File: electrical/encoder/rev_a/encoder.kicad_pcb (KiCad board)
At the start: 2 copper layers, 19.8 x 45.5 mm, 1 part, among them CN1 HR2_Encoder;HR2Encoder

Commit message: Finally have everything fitting together.
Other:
- board size 19.8 x 45.5 mm -> 14.8 x 40.4 mm

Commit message: Started working on encdoer PCB.
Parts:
- added Q1: AH1806;SC59, HR2:SC59, F.Cu at (101.1, 81.0)
- CN1: value HR2_Encoder;HR2Encoder -> ENCODER;2xM1x3RA; footprint HR2:Encoder -> HR2:ENCODER_2xM1x3RA
- moved CN1 3.31 mm to (96.7, 100.3)
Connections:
- CN1 pad 1: (no net) -> Net-(CN1-Pad1)
- CN1 pad 2: (no net) -> Net-(CN1-Pad2)
- CN1 pad 3: (no net) -> Net-(CN1-Pad3)
- CN1 pad 4: (no net) -> Net-(CN1-Pad4)
- CN1 pad 5: (no net) -> Net-(CN1-Pad5)
- CN1 pad 6: (no net) -> Net-(CN1-Pad6)
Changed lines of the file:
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@@
-(kicad_pcb (version 20171130) (host pcbnew 5.1.6-c6e7f7d~86~ubuntu18.04.1)
+(kicad_pcb (version 20171130) (host pcbnew 5.1.6-c6e7f7d~87~ubuntu18.04.1)
   (general
     (thickness 1.6)
@@
     (tracks 0)
     (zones 0)
-    (modules 1)
-    (nets 1)
+    (modules 2)
+    (nets 10)
   )
   (page A4)
@@
   )
   (net 0 "")
+  (net 1 "Net-(CN1-Pad3)")
+  (net 2 "Net-(CN1-Pad2)")
+  (net 3 "Net-(CN1-Pad1)")
+  (net 4 "Net-(CN1-Pad6)")
+  (net 5 "Net-(CN1-Pad5)")
+  (net 6 "Net-(CN1-Pad4)")
+  (net 7 "Net-(Q1-Pad2)")
+  (net 8 "Net-(Q1-Pad1)")
+  (net 9 "Net-(Q1-Pad3)")
   (net_class Default "This is the default net class."
     (clearance 0.2)
@@
     (uvia_dia 0.3)
     (uvia_drill 0.1)
+    (add_net "Net-(CN1-Pad1)")
+    (add_net "Net-(CN1-Pad2)")
+    (add_net "Net-(CN1-Pad3)")
+    (add_net "Net-(CN1-Pad4)")
+    (add_net "Net-(CN1-Pad5)")
+    (add_net "Net-(CN1-Pad6)")
+    (add_net "Net-(Q1-Pad1)")
+    (add_net "Net-(Q1-Pad2)")
+    (add_net "Net-(Q1-Pad3)")
   )
-  (module HR2:Encoder (layer F.Cu)
-    (at 100.00 100.00)
-    (fp_text reference CN1 (at -10.7 20.5) (layer F.SilkS)
+  (module HR2:SC59 (layer F.Cu)
+    (at 101.101623 80.969999)
+    (fp_text reference Q1 (at 1.27 7.62) (layer F.SilkS)
+      (effects (font (size 1 1) (thickness 0.15)))
+    )
+    (fp_text value AH1806;SC59 (at 0 -11.43) (layer F.Fab)
+      (effects (font (size 1 1) (thickness 0.15)))
+    )
+    (fp_line (start -1.5 -0.8) (end -1.5 0.8) (layer F.SilkS) (width 0.1))
+    (fp_line (start -1.5 -0.8) (end 1.5 -0.8) (layer F.SilkS) (width 0.1))
+    (fp_line (start -1.5 0.8) (end 1.5 0.8) (layer F.SilkS) (width 0.1))
+    (fp_line (start 1.5 -0.8) (end 1.5 0.8) (layer F.SilkS) (width 0.1))
+    (fp_circle (center -1.67 0.94) (end -1.66 0.91) (layer F.SilkS) (width 0.1))
+    (pad 2 smd rect (at 0 -1.2) (size 0.8 1) (layers F.Cu F.Paste F.Mask)
+      (net 7 "Net-(Q1-Pad2)"))
+    (pad 1 smd rect (at -0.95 1.2) (size 0.8 1) (layers F.Cu F.Paste F.Mask)
+      (net 8 "Net-(Q1-Pad1)"))
+    (pad 3 smd rect (at 0.95 1.2) (size 0.8 1) (layers F.Cu F.Paste F.Mask)
+      (net 9 "Net-(Q1-Pad3)"))
+  )
+  (module HR2:ENCODER_2xM1x3RA (layer F.Cu)
+    (at 96.7 100.3)
+    (fp_text reference CN1 (at 0 -2) (layer F.SilkS)
       (effects (font (size 1 1) (thickness 0.2)))
     )
-    (fp_text value HR2_Encoder;HR2Encoder (at 0 -2) (layer F.Fab)
+    (fp_text value ENCODER;2xM1x3RA (at 0 0) (layer F.Fab)
       (effects (font (size 1 1) (thickness 0.2)))
     )
-    (fp_line (start -5.5731 -21.46) (end -3.0331 -21.46) (layer B.SilkS) (width 0.2))
-    (fp_line (start -3.0331 -21.46) (end -3.0331 -13.84) (layer B.SilkS) (width 0.2))
-    (fp_line (start -3.0331 -13.84) (end -5.5731 -13.84) (layer B.SilkS) (width 0.2))
-    (fp_line (start -5.5731 -13.84) (end -5.5731 -21.46) (layer B.SilkS) (width 0.2))
-    (fp_line (start -6.7181 -15.11) (end -5.5731 -15.11) (layer B.SilkS) (width 0.2))
-    (fp_line (start -6.7181 -17.65) (end -5.5731 -17.65) (layer B.SilkS) (width 0.2))
-    (fp_line (start -6.7181 -20.19) (end -5.5731 -20.19) (layer B.SilkS) (width 0.2))
-    (fp_line (start -9.3851 -13.305) (end -9.4558 -13.2757) (layer B.SilkS) (width 0.2))
-    (fp_line (start -9.4558 -13.2757) (end -9.4851 -13.205) (layer B.SilkS) (width 0.2))
-    (fp_line (start -9.4851 -13.205) (end -9.4558 -13.1343) (layer B.SilkS) (width 0.2))
-    (fp_line (start -9.4558 -13.1343) (end -9.3851 -13.105) (layer B.SilkS) (width 0.2))
-    (fp_line (start -9.3851 -13.105) (end -9.3144 -13.1343) (layer B.SilkS) (width 0.2))
-    (fp_line (start -9.3144 -13.1343) (end -9.2851 -13.205) (layer B.SilkS) (width 0.2))
-    (fp_line (start -9.2851 -13.205) (end -9.3144 -13.2757) (layer B.SilkS) (width 0.2))
-    (fp_line (start -9.3144 -13.2757) (end -9.3851 -13.305) (layer B.SilkS) (width 0.2))
-    (fp_line (start -5.5731 13.84) (end -3.0331 13.84) (layer B.SilkS) (width 0.2))
-    (fp_line (start -3.0331 13.84) (end -3.0331 21.46) (layer B.SilkS) (width 0.2))
-    (fp_line (start -3.0331 21.46) (end -5.5731 21.46) (layer B.SilkS) (width 0.2))
-    (fp_line (start -5.5731 21.46) (end -5.5731 13.84) (layer B.SilkS) (width 0.2))
-    (fp_line (start -6.7181 20.19) (end -5.5731 20.19) (layer B.SilkS) (width 0.2))
-    (fp_line (start -6.7181 17.65) (end -5.5731 17.65) (layer B.SilkS) (width 0.2))
-    (fp_line (start -6.7181 15.11) (end -5.5731 15.11) (layer B.SilkS) (width 0.2))
-    (fp_line (start -9.3851 21.995) (end -9.4558 22.0243) (layer B.SilkS) (width 0.2))
-    (fp_line (start -9.4558 22.0243) (end -9.4851 22.095) (layer B.SilkS) (width 0.2))
-    (fp_line (start -9.4851 22.095) (end -9.4558 22.1657) (layer B.SilkS) (width 0.2))
-    (fp_line (start -9.4558 22.1657) (end -9.3851 22.195) (layer B.SilkS) (width 0.2))
-    (fp_line (start -9.3851 22.195) (end -9.3144 22.1657) (layer B.SilkS) (width 0.2))
-    (fp_line (start -9.3144 22.1657) (end -9.2851 22.095) (layer B.SilkS) (width 0.2))
-    (fp_line (start -9.2851 22.095) (end -9.3144 22.0243) (layer B.SilkS) (width 0.2))
-    (fp_line (start -9.3144 22.0243) (end -9.3851 21.995) (layer B.SilkS) (width 0.2))
-    (pad 7 thru_hole oval (at 0 6.6252) (size 3.3 1.7) (drill oval 2.6 0.9) (layers *.Cu *.Mask))
-    (pad 8 thru_hole oval (at 0 -6.6248) (size 3.3 1.7) (drill oval 2.6 0.9) (layers *.Cu *.Mask))
-    (pad 1 thru_hole circle (at -7.4801 20.19) (size 1.5 1.5) (drill 1) (layers *.Cu *.Mask))
-    (pad 2 thru_hole circle (at -7.4801 17.65) (size 1.5 1.5) (drill 1) (layers *.Cu *.Mask))
-    (pad 3 thru_hole circle (at -7.4801 15.11) (size 1.5 1.5) (drill 1) (layers *.Cu *.Mask))
-    (pad 4 thru_hole circle (at -7.4801 -15.11) (size 1.5 1.5) (drill 1) (layers *.Cu *.Mask))
-    (pad 5 thru_hole circle (at -7.4801 -17.65) (size 1.5 1.5) (drill 1) (layers *.Cu *.Mask))
-    (pad 6 thru_hole circle (at -7.4801 -20.19) (size 1.5 1.5) (drill 1) (layers *.Cu *.Mask))
+    (fp_line (start -9.39 -12.57) (end -11.93 -12.57) (layer B.SilkS) (width 0.2))
+    (fp_line (start -11.93 -12.57) (end -11.93 -20.19) (layer B.SilkS) (width 0.2))
+    (fp_line (start -11.93 -20.19) (end -9.39 -20.19) (layer B.SilkS) (width 0.2))
+    (fp_line (start -9.39 -20.19) (end -9.39 -12.57) (layer B.SilkS) (width 0.2))
+    (fp_line (start -8.24 -18.92) (end -9.39 -18.92) (layer B.SilkS) (width 0.2))
+    (fp_line (start -8.24 -16.38) (end -9.39 -16.38) (layer B.SilkS) (width 0.2))
+    (fp_line (start -8.24 -13.84) (end -9.39 -13.84) (layer B.SilkS) (width 0.2))
+    (fp_line (start -8.75 -20.73) (end -8.68 -20.75) (layer B.SilkS) (width 0.2))
+    (fp_line (start -8.68 -20.75) (end -8.65 -20.83) (layer B.SilkS) (width 0.2))
+    (fp_line (start -8.65 -20.83) (end -8.68 -20.9) (layer B.SilkS) (width 0.2))
+    (fp_line (start -8.68 -20.9) (end -8.75 -20.93) (layer B.SilkS) (width 0.2))
+    (fp_line (start -8.75 -20.93) (end -8.82 -20.9) (layer B.SilkS) (width 0.2))
+    (fp_line (start -8.82 -20.9) (end -8.85 -20.83) (layer B.SilkS) (width 0.2))
+    (fp_line (start -8.85 -20.83) (end -8.82 -20.75) (layer B.SilkS) (width 0.2))
+    (fp_line (start -8.82 -20.75) (end -8.75 -20.73) (layer B.SilkS) (width 0.2))
+    (fp_line (start -9.39 20.19) (end -11.93 20.19) (layer B.SilkS) (width 0.2))
+    (fp_line (start -11.93 20.19) (end -11.93 12.57) (layer B.SilkS) (width 0.2))
+    (fp_line (start -11.93 12.57) (end -9.39 12.57) (layer B.SilkS) (width 0.2))
+    (fp_line (start -9.39 12.57) (end -9.39 20.19) (layer B.SilkS) (width 0.2))
+    (fp_line (start -8.24 13.84) (end -9.39 13.84) (layer B.SilkS) (width 0.2))
+    (fp_line (start -8.24 16.38) (end -9.39 16.38) (layer B.SilkS) (width 0.2))
+    (fp_line (start -8.24 18.92) (end -9.39 18.92) (layer B.SilkS) (width 0.2))
+    (fp_line (start -8.75 12.04) (end -8.68 12.01) (layer B.SilkS) (width 0.2))
+    (fp_line (start -8.68 12.01) (end -8.65 11.94) (layer B.SilkS) (width 0.2))
+    (fp_line (start -8.65 11.94) (end -8.68 11.86) (layer B.SilkS) (width 0.2))
+    (fp_line (start -8.68 11.86) (end -8.75 11.84) (layer B.SilkS) (width 0.2))
+    (fp_line (start -8.75 11.84) (end -8.82 11.86) (layer B.SilkS) (width 0.2))
+    (fp_line (start -8.82 11.86) (end -8.85 11.94) (layer B.SilkS) (width 0.2))
+    (fp_line (start -8.85 11.94) (end -8.82 12.01) (layer B.SilkS) (width 0.2))
+    (fp_line (start -8.82 12.01) (end -8.75 12.04) (layer B.SilkS) (width 0.2))
+    (pad "Encoder Shaft Hole" np_thru_hole circle (at 0 0) (size 3 3) (drill 3) (layers *.Cu *.Mask))
+    (pad 7 thru_hole oval (at 0 6.6252) (size 3.3 1.65) (drill oval 2.55 0.9) (layers *.Cu *.Mask))
+    (pad 8 thru_hole oval (at 0 -6.6248) (size 3.3 1.65) (drill oval 2.55 0.9) (layers *.Cu *.Mask))
+    (pad 3 thru_hole circle (at -7.4801 13.84) (size 1.52 1.52) (drill 1.02) (layers *.Cu *.Mask)
+      (net 1 "Net-(CN1-Pad3)"))
+    (pad 2 thru_hole circle (at -7.4801 16.38) (size 1.52 1.52) (drill 1.02) (layers *.Cu *.Mask)
+      (net 2 "Net-(CN1-Pad2)"))
+    (pad 1 thru_hole circle (at -7.4801 18.92) (size 1.52 1.52) (drill 1.02) (layers *.Cu *.Mask)
+      (net 3 "Net-(CN1-Pad1)"))
+    (pad 6 thru_hole circle (at -7.4801 -18.92) (size 1.52 1.52) (drill 1.02) (layers *.Cu *.Mask)
+      (net 4 "Net-(CN1-Pad6)"))
+    (pad 5 thru_hole circle (at -7.4801 -16.38) (size 1.52 1.52) (drill 1.02) (layers *.Cu *.Mask)
+      (net 5 "Net-(CN1-Pad5)"))
+    (pad 4 thru_hole circle (at -7.4801 -13.84) (size 1.52 1.52) (drill 1.02) (layers *.Cu *.Mask)
+      (net 6 "Net-(CN1-Pad4)"))
   )
   (gr_line (start 92.5 79.81) (end 92.37 79.82) (layer Edge.Cuts) (width 0.05))

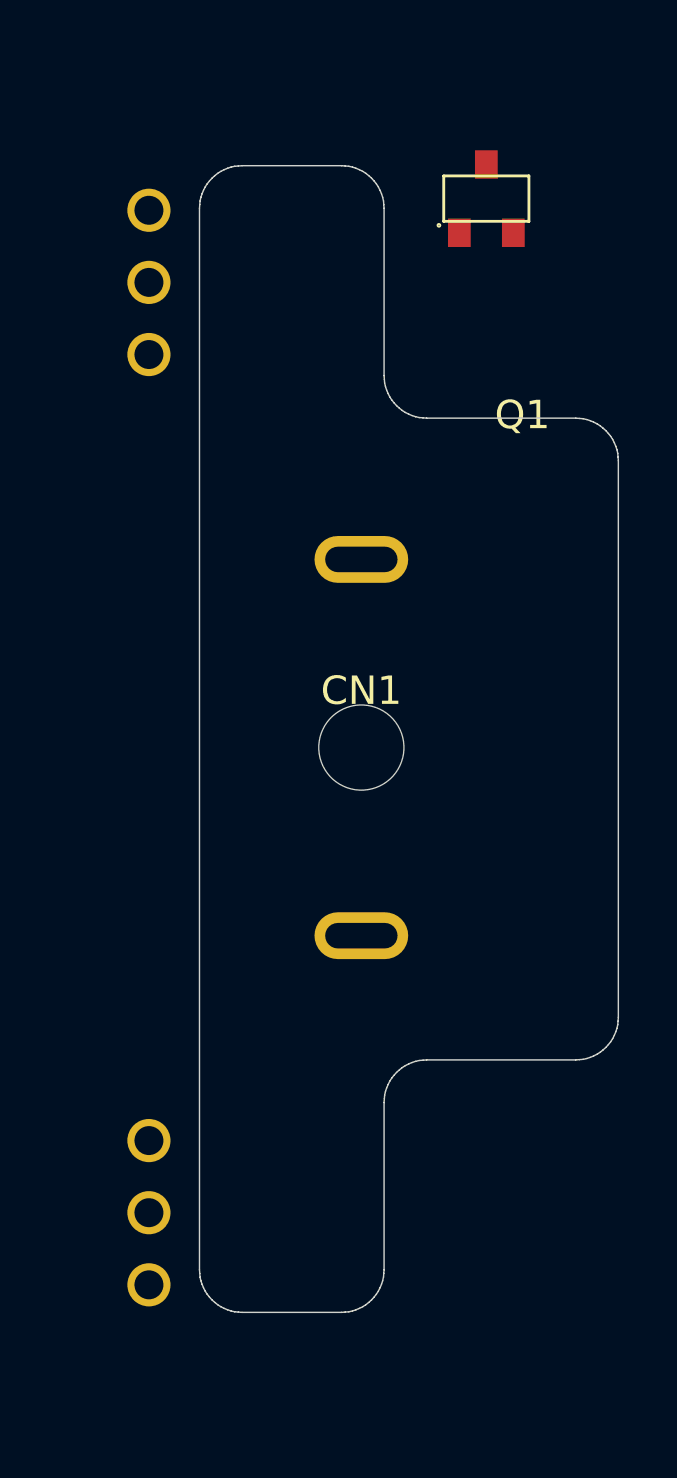
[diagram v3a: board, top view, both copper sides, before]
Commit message: Found and fixed nasty bug in Square class.
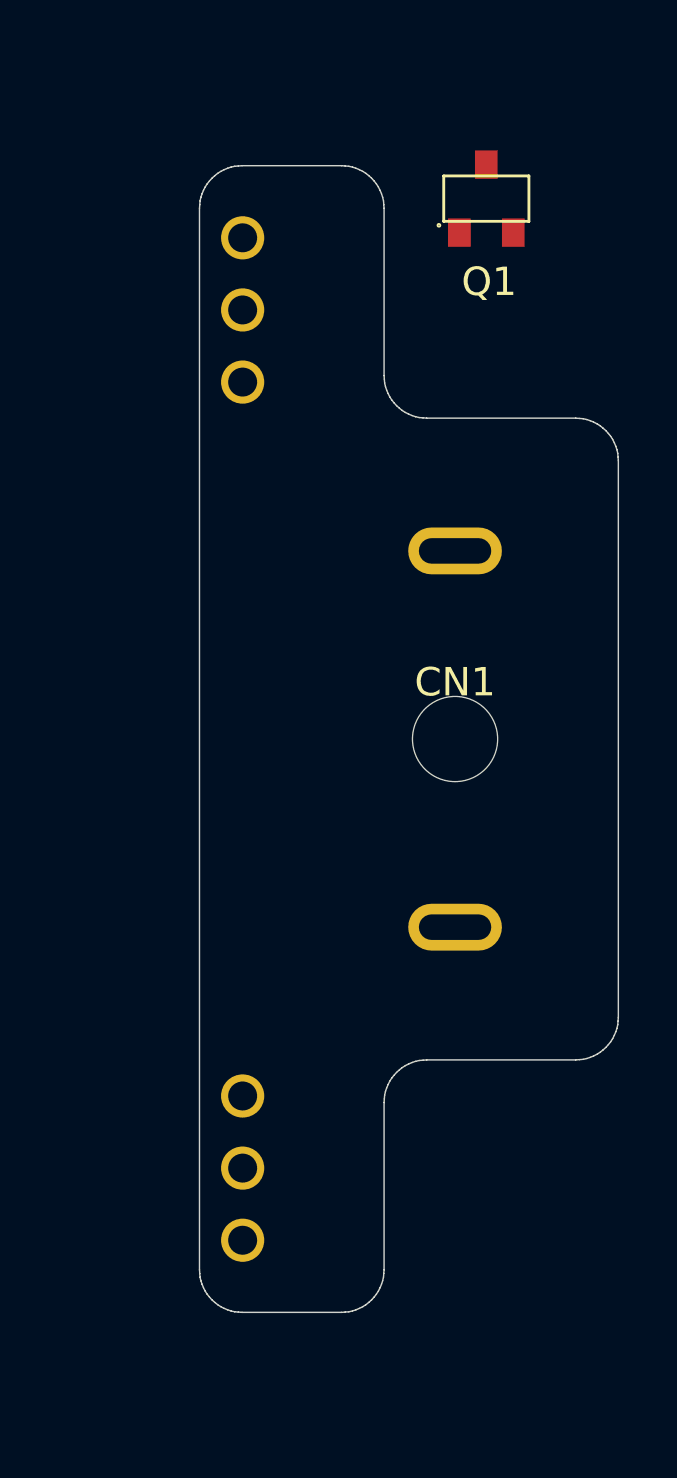
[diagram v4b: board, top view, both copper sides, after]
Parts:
- moved CN1 3.31 mm to (100.0, 100.0)
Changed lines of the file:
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@@
   (module HR2:SC59 (layer F.Cu)
     (at 101.101623 80.969999)
-    (fp_text reference Q1 (at 1.27 7.62) (layer F.SilkS)
+    (fp_text reference Q1 (at 0.098377 2.930001) (layer F.SilkS)
       (effects (font (size 1 1) (thickness 0.15)))
     )
@@
   )
   (module HR2:ENCODER_2xM1x3RA (layer F.Cu)
-    (at 96.7 100.3)
+    (at 100 100)
     (fp_text reference CN1 (at 0 -2) (layer F.SilkS)
       (effects (font (size 1 1) (thickness 0.2)))
@@
       (effects (font (size 1 1) (thickness 0.2)))
     )
-    (fp_line (start -9.39 -12.57) (end -11.93 -12.57) (layer B.SilkS) (width 0.2))
-    (fp_line (start -11.93 -12.57) (end -11.93 -20.19) (layer B.SilkS) (width 0.2))
-    (fp_line (start -11.93 -20.19) (end -9.39 -20.19) (layer B.SilkS) (width 0.2))
-    (fp_line (start -9.39 -20.19) (end -9.39 -12.57) (layer B.SilkS) (width 0.2))
-    (fp_line (start -8.24 -18.92) (end -9.39 -18.92) (layer B.SilkS) (width 0.2))
-    (fp_line (start -8.24 -16.38) (end -9.39 -16.38) (layer B.SilkS) (width 0.2))
-    (fp_line (start -8.24 -13.84) (end -9.39 -13.84) (layer B.SilkS) (width 0.2))
-    (fp_line (start -8.75 -20.73) (end -8.68 -20.75) (layer B.SilkS) (width 0.2))
-    (fp_line (start -8.68 -20.75) (end -8.65 -20.83) (layer B.SilkS) (width 0.2))
-    (fp_line (start -8.65 -20.83) (end -8.68 -20.9) (layer B.SilkS) (width 0.2))
-    (fp_line (start -8.68 -20.9) (end -8.75 -20.93) (layer B.SilkS) (width 0.2))
-    (fp_line (start -8.75 -20.93) (end -8.82 -20.9) (layer B.SilkS) (width 0.2))
-    (fp_line (start -8.82 -20.9) (end -8.85 -20.83) (layer B.SilkS) (width 0.2))
-    (fp_line (start -8.85 -20.83) (end -8.82 -20.75) (layer B.SilkS) (width 0.2))
-    (fp_line (start -8.82 -20.75) (end -8.75 -20.73) (layer B.SilkS) (width 0.2))
-    (fp_line (start -9.39 20.19) (end -11.93 20.19) (layer B.SilkS) (width 0.2))
-    (fp_line (start -11.93 20.19) (end -11.93 12.57) (layer B.SilkS) (width 0.2))
-    (fp_line (start -11.93 12.57) (end -9.39 12.57) (layer B.SilkS) (width 0.2))
-    (fp_line (start -9.39 12.57) (end -9.39 20.19) (layer B.SilkS) (width 0.2))
-    (fp_line (start -8.24 13.84) (end -9.39 13.84) (layer B.SilkS) (width 0.2))
-    (fp_line (start -8.24 16.38) (end -9.39 16.38) (layer B.SilkS) (width 0.2))
-    (fp_line (start -8.24 18.92) (end -9.39 18.92) (layer B.SilkS) (width 0.2))
-    (fp_line (start -8.75 12.04) (end -8.68 12.01) (layer B.SilkS) (width 0.2))
-    (fp_line (start -8.68 12.01) (end -8.65 11.94) (layer B.SilkS) (width 0.2))
-    (fp_line (start -8.65 11.94) (end -8.68 11.86) (layer B.SilkS) (width 0.2))
-    (fp_line (start -8.68 11.86) (end -8.75 11.84) (layer B.SilkS) (width 0.2))
-    (fp_line (start -8.75 11.84) (end -8.82 11.86) (layer B.SilkS) (width 0.2))
-    (fp_line (start -8.82 11.86) (end -8.85 11.94) (layer B.SilkS) (width 0.2))
-    (fp_line (start -8.85 11.94) (end -8.82 12.01) (layer B.SilkS) (width 0.2))
-    (fp_line (start -8.82 12.01) (end -8.75 12.04) (layer B.SilkS) (width 0.2))
+    (fp_line (start -5.57 -18.92) (end -5.57 -11.3) (layer B.SilkS) (width 0.2))
+    (fp_line (start -5.57 -11.3) (end -3.03 -11.3) (layer B.SilkS) (width 0.2))
+    (fp_line (start -3.03 -11.3) (end -3.03 -18.92) (layer B.SilkS) (width 0.2))
+    (fp_line (start -3.03 -18.92) (end -5.57 -18.92) (layer B.SilkS) (width 0.2))
+    (fp_line (start -6.72 -12.57) (end -5.57 -12.57) (layer B.SilkS) (width 0.2))
+    (fp_line (start -6.72 -15.11) (end -5.57 -15.11) (layer B.SilkS) (width 0.2))
+    (fp_line (start -6.72 -17.65) (end -5.57 -17.65) (layer B.SilkS) (width 0.2))
+    (fp_line (start -6.21 -10.77) (end -6.28 -10.74) (layer B.SilkS) (width 0.2))
+    (fp_line (start -6.28 -10.74) (end -6.31 -10.67) (layer B.SilkS) (width 0.2))
+    (fp_line (start -6.31 -10.67) (end -6.28 -10.59) (layer B.SilkS) (width 0.2))
+    (fp_line (start -6.28 -10.59) (end -6.21 -10.57) (layer B.SilkS) (width 0.2))
+    (fp_line (start -6.21 -10.57) (end -6.14 -10.59) (layer B.SilkS) (width 0.2))
+    (fp_line (start -6.14 -10.59) (end -6.11 -10.67) (layer B.SilkS) (width 0.2))
+    (fp_line (start -6.11 -10.67) (end -6.14 -10.74) (layer B.SilkS) (width 0.2))
+    (fp_line (start -6.14 -10.74) (end -6.21 -10.77) (layer B.SilkS) (width 0.2))
+    (fp_line (start -5.57 11.3) (end -5.57 18.92) (layer B.SilkS) (width 0.2))
+    (fp_line (start -5.57 18.92) (end -3.03 18.92) (layer B.SilkS) (width 0.2))
+    (fp_line (start -3.03 18.92) (end -3.03 11.3) (layer B.SilkS) (width 0.2))
+    (fp_line (start -3.03 11.3) (end -5.57 11.3) (layer B.SilkS) (width 0.2))
+    (fp_line (start -6.72 17.65) (end -5.57 17.65) (layer B.SilkS) (width 0.2))
+    (fp_line (start -6.72 15.11) (end -5.57 15.11) (layer B.SilkS) (width 0.2))
+    (fp_line (start -6.72 12.57) (end -5.57 12.57) (layer B.SilkS) (width 0.2))
+    (fp_line (start -6.21 19.46) (end -6.28 19.48) (layer B.SilkS) (width 0.2))
+    (fp_line (start -6.28 19.48) (end -6.31 19.56) (layer B.SilkS) (width 0.2))
+    (fp_line (start -6.31 19.56) (end -6.28 19.63) (layer B.SilkS) (width 0.2))
+    (fp_line (start -6.28 19.63) (end -6.21 19.66) (layer B.SilkS) (width 0.2))
+    (fp_line (start -6.21 19.66) (end -6.14 19.63) (layer B.SilkS) (width 0.2))
+    (fp_line (start -6.14 19.63) (end -6.11 19.56) (layer B.SilkS) (width 0.2))
+    (fp_line (start -6.11 19.56) (end -6.14 19.48) (layer B.SilkS) (width 0.2))
+    (fp_line (start -6.14 19.48) (end -6.21 19.46) (layer B.SilkS) (width 0.2))
     (pad "Encoder Shaft Hole" np_thru_hole circle (at 0 0) (size 3 3) (drill 3) (layers *.Cu *.Mask))
     (pad 7 thru_hole oval (at 0 6.6252) (size 3.3 1.65) (drill oval 2.55 0.9) (layers *.Cu *.Mask))
     (pad 8 thru_hole oval (at 0 -6.6248) (size 3.3 1.65) (drill oval 2.55 0.9) (layers *.Cu *.Mask))
-    (pad 3 thru_hole circle (at -7.4801 13.84) (size 1.52 1.52) (drill 1.02) (layers *.Cu *.Mask)
+    (pad 3 thru_hole circle (at -7.4801 12.57) (size 1.52 1.52) (drill 1.02) (layers *.Cu *.Mask)
       (net 1 "Net-(CN1-Pad3)"))
-    (pad 2 thru_hole circle (at -7.4801 16.38) (size 1.52 1.52) (drill 1.02) (layers *.Cu *.Mask)
+    (pad 2 thru_hole circle (at -7.4801 15.11) (size 1.52 1.52) (drill 1.02) (layers *.Cu *.Mask)
       (net 2 "Net-(CN1-Pad2)"))
-    (pad 1 thru_hole circle (at -7.4801 18.92) (size 1.52 1.52) (drill 1.02) (layers *.Cu *.Mask)
+    (pad 1 thru_hole circle (at -7.4801 17.65) (size 1.52 1.52) (drill 1.02) (layers *.Cu *.Mask)
       (net 3 "Net-(CN1-Pad1)"))
-    (pad 6 thru_hole circle (at -7.4801 -18.92) (size 1.52 1.52) (drill 1.02) (layers *.Cu *.Mask)
+    (pad 6 thru_hole circle (at -7.4801 -17.65) (size 1.52 1.52) (drill 1.02) (layers *.Cu *.Mask)
       (net 4 "Net-(CN1-Pad6)"))
-    (pad 5 thru_hole circle (at -7.4801 -16.38) (size 1.52 1.52) (drill 1.02) (layers *.Cu *.Mask)
+    (pad 5 thru_hole circle (at -7.4801 -15.11) (size 1.52 1.52) (drill 1.02) (layers *.Cu *.Mask)
       (net 5 "Net-(CN1-Pad5)"))
-    (pad 4 thru_hole circle (at -7.4801 -13.84) (size 1.52 1.52) (drill 1.02) (layers *.Cu *.Mask)
+    (pad 4 thru_hole circle (at -7.4801 -12.57) (size 1.52 1.52) (drill 1.02) (layers *.Cu *.Mask)
       (net 6 "Net-(CN1-Pad4)"))
   )

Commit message: Wrapped up encoder PCB.
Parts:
- added Q2: AH1806;SC59, HR2:SC59, F.Cu at (96.6, 103.4)
- added R1: 100Ω;1608, Resistor_SMD:R_0603_1608Metric, F.Cu at (94.9, 108.5)
- added R2: 100Ω;1608, Resistor_SMD:R_0603_1608Metric, F.Cu at (92.5, 94.0)
- moved Q1 16.2 mm to (96.6, 96.6), turned to 135 degrees
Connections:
- CN1 pad 1: Net-(CN1-Pad1) -> /GND
- CN1 pad 2: Net-(CN1-Pad2) -> /QUADA
- CN1 pad 3: Net-(CN1-Pad3) -> /QUADB
- CN1 pad 4: Net-(CN1-Pad4) -> /VCC
- CN1 pad 5: Net-(CN1-Pad5) -> /MOTOR+
- CN1 pad 6: Net-(CN1-Pad6) -> /MOTOR-
- CN1 pad 7: (no net) -> /MOTOR-
- CN1 pad 8: (no net) -> /MOTOR+
- Q1 pad 1: Net-(Q1-Pad1) -> /VCC
- Q1 pad 2: Net-(Q1-Pad2) -> /GND
- Q1 pad 3: Net-(Q1-Pad3) -> /QUADB
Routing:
- net /VCC: track 0.00 -> 35.8 mm
- net /GND: track 0.00 -> 35.1 mm, vias 0 -> 4
- net /MOTOR-: track 0.00 -> 33.1 mm
- net /QUADB: track 0.00 -> 22.7 mm
- net /QUADA: track 0.00 -> 20.2 mm
- net /MOTOR+: track 0.00 -> 12.9 mm
- added copper zone on B.Cu, net /GND
- added copper zone on F.Cu, net /GND
